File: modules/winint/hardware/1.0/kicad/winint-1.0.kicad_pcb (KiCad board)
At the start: 2 copper layers, 75 x 75 mm, 43 parts, among them J1 NPN SENSOR, J2 Screw_Terminal_01x05, J3 M12-5PIN, J4 RELAYS, K1 SANYOU_SRD_Form_C, K2 SANYOU_SRD_Form_C, Q1 2N2219, Q2 2N2219, SW1 INSTANCE, U1 CNY74-4H, U2 Teensy_3.2, U3 TEC2-2411WI, U4 MCP2551-I-P

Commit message: Refactor again
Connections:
- U2 pad 10: Net-(U1-Pad15) -> Net-(R8-Pad1)
- U2 pad 11: Net-(U1-Pad14) -> Net-(U1-Pad15)
- U2 pad 12: Net-(R8-Pad1) -> Net-(U1-Pad14)
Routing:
- net Net-(R8-Pad1): track 116.8 -> 121.9 mm
- net Net-(U1-Pad15): track 65.1 -> 67.8 mm
- net Net-(U1-Pad14): track 68.5 -> 71.0 mm

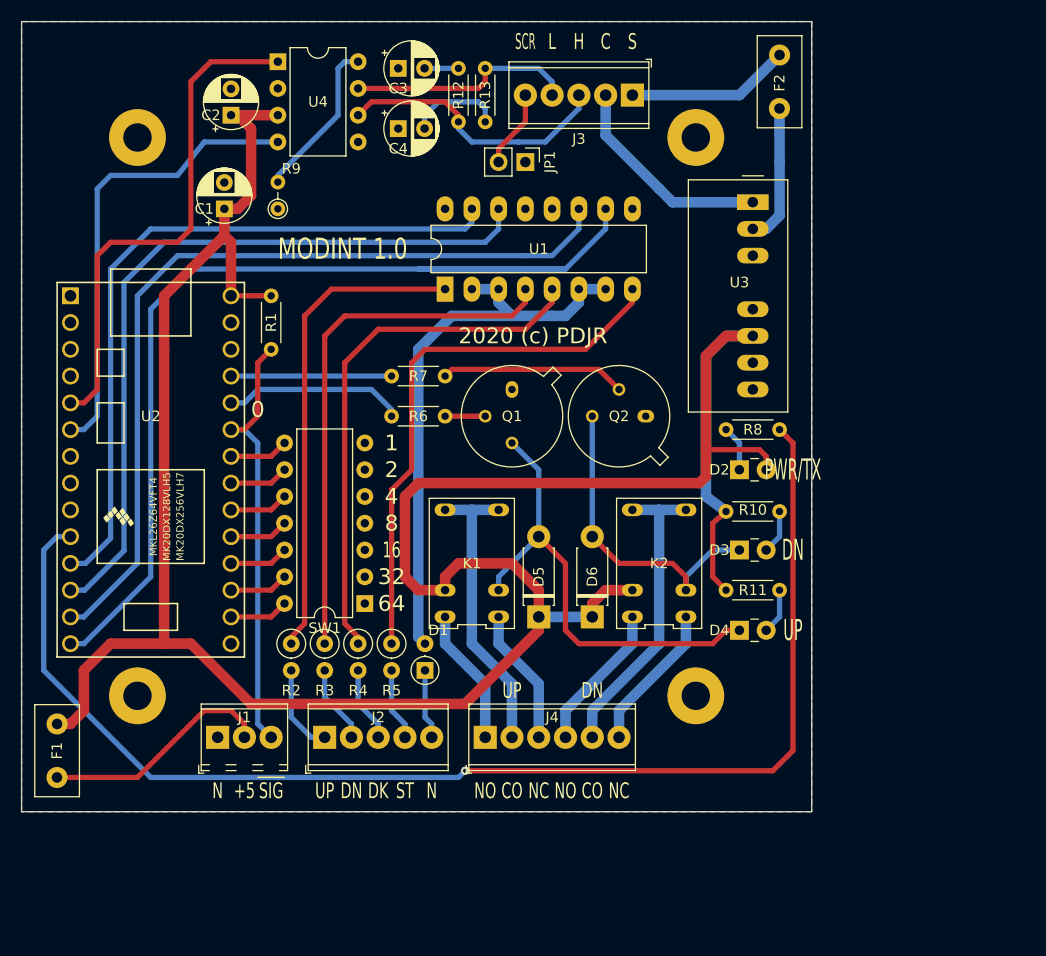
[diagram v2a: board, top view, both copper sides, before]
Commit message: Added 12V fused supply and OPTO isolation to rotation sensor input
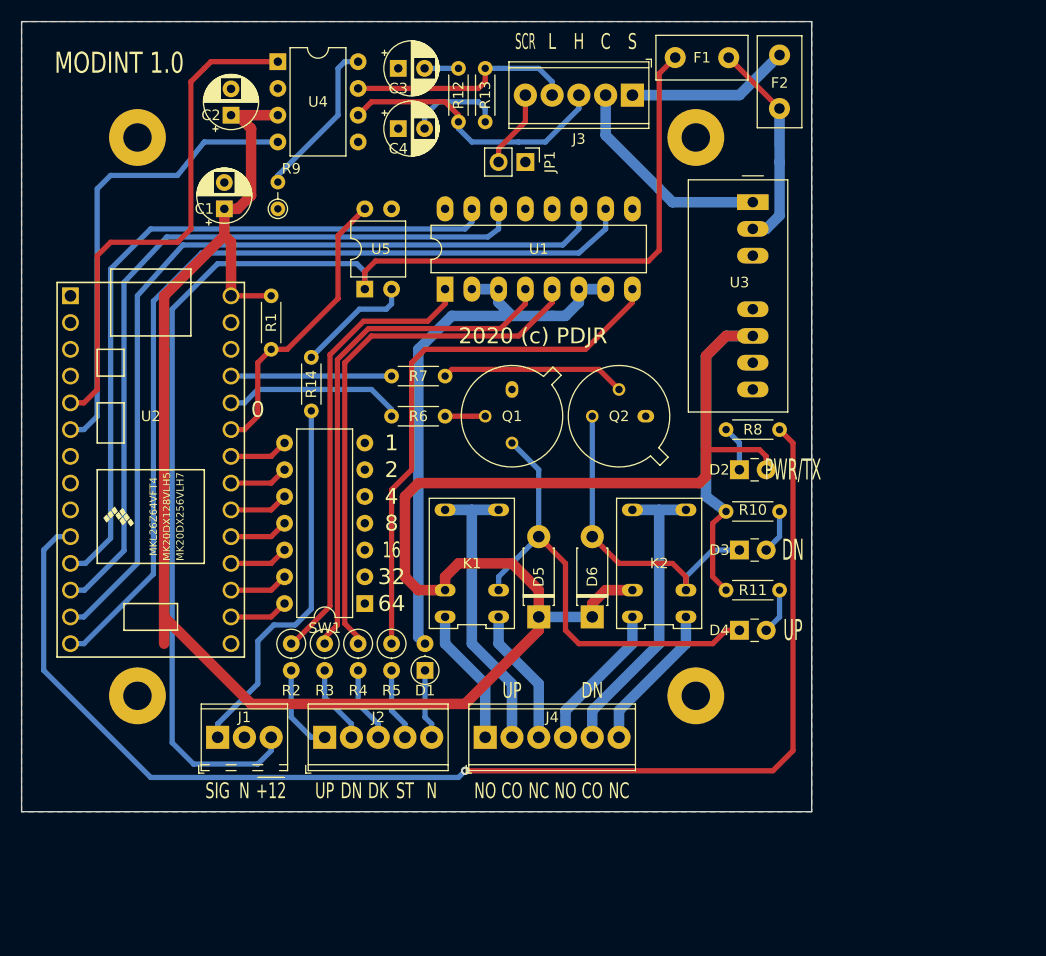
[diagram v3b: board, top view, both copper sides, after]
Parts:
- added R14: 1K, Resistor_THT:R_Axial_DIN0204_L3.6mm_D1.6mm_P5.08mm_Horizontal, F.Cu at (163.5, 124.0)
- added U5: PC817, Package_DIP:DIP-4_W7.62mm, F.Cu at (168.6, 112.4)
- R1: value 4K7 -> 10K
- moved F1 89.8 mm to (203.1, 90.4), turned to 180 degrees
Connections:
- F1 pad 1: Net-(C1-Pad1) -> Net-(F1-Pad1)
- F2 pad 2: Net-(F2-Pad2) -> Net-(F1-Pad1)
- J1 pad 1: GND -> Net-(J1-Pad1)
- J1 pad 2: Net-(F1-Pad2) -> GND
- J1 pad 3: Net-(J1-Pad3) -> Net-(F1-Pad2)
- R1 pad 1: Net-(J1-Pad3) -> Net-(R1-Pad1)
- U2 pad 23: Net-(J1-Pad3) -> Net-(R1-Pad1)
- U3 pad 2: Net-(F2-Pad2) -> Net-(F1-Pad1)
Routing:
- net Net-(F1-Pad2): track 22.2 -> 124.6 mm
- net Net-(J1-Pad3): track 41.5 -> 0.00 mm
- net Net-(J1-Pad1): track 0.00 -> 35.9 mm
- net Net-(R1-Pad1): track 0.00 -> 27.9 mm
- net Net-(F1-Pad1): track 0.00 -> 20.1 mm
- net Net-(C1-Pad1): track 247.1 -> 232.6 mm
- net Net-(U1-Pad10): track 97.2 -> 83.5 mm
- net Net-(F2-Pad2): track 13.2 -> 0.00 mm
- net Net-(R14-Pad2): track 0.00 -> 11.1 mm
- net Net-(R2-Pad1): track 46.0 -> 43.3 mm
- net Net-(R3-Pad1): track 50.8 -> 48.9 mm
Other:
- board text added: "+12"
- board text removed: "+5"

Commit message: Revised for mult-mode inputs
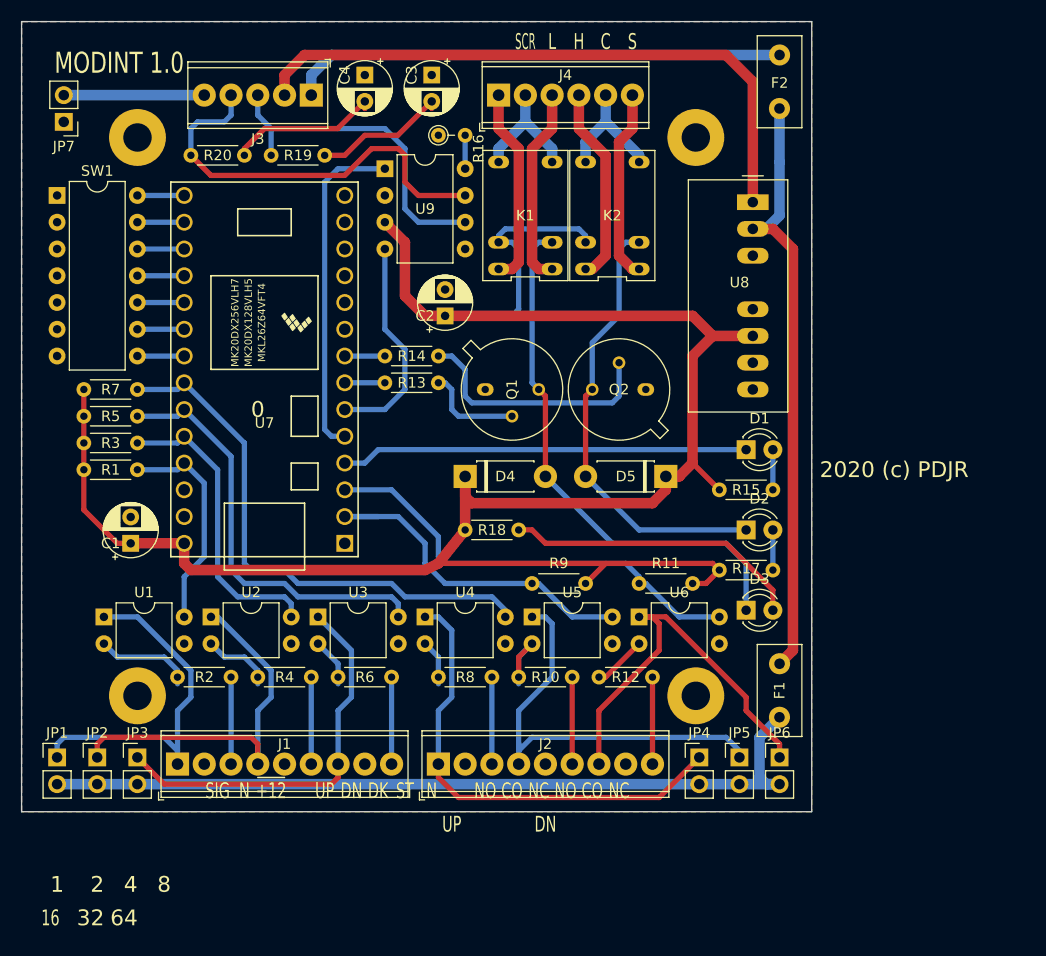
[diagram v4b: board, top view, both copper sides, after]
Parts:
- removed the D1 at (174.3, 148.6)
- removed the R13 at (180.0, 96.5)
- removed the R14 at (163.5, 124.0)
- added JP1: SCR, Connector_PinHeader_2.54mm:PinHeader_1x02_P2.54mm_Vertical, F.Cu at (139.4, 156.8)
- added JP2: SCR, Connector_PinHeader_2.54mm:PinHeader_1x02_P2.54mm_Vertical, F.Cu at (143.2, 156.8)
- added JP3: SCR, Connector_PinHeader_2.54mm:PinHeader_1x02_P2.54mm_Vertical, F.Cu at (147.0, 156.8)
- added JP4: SCR, Connector_PinHeader_2.54mm:PinHeader_1x02_P2.54mm_Vertical, F.Cu at (200.3, 156.8)
- added JP5: SCR, Connector_PinHeader_2.54mm:PinHeader_1x02_P2.54mm_Vertical, F.Cu at (204.1, 156.8)
- added JP6: SCR, Connector_PinHeader_2.54mm:PinHeader_1x02_P2.54mm_Vertical, F.Cu at (207.9, 156.8)
- added R10: 1.4K, Resistor_THT:R_Axial_DIN0204_L3.6mm_D1.6mm_P5.08mm_Horizontal, F.Cu at (183.2, 149.2)
- added R11: 10K, Resistor_THT:R_Axial_DIN0204_L3.6mm_D1.6mm_P5.08mm_Horizontal, F.Cu at (194.6, 140.3)
- added R12: 1.4K, Resistor_THT:R_Axial_DIN0204_L3.6mm_D1.6mm_P5.08mm_Horizontal, F.Cu at (190.8, 149.2)
- added R20: 100R, Resistor_THT:R_Axial_DIN0204_L3.6mm_D1.6mm_P5.08mm_Horizontal, F.Cu at (157.2, 99.7)
- added R6: 1.4K, Resistor_THT:R_Axial_DIN0204_L3.6mm_D1.6mm_P5.08mm_Horizontal, F.Cu at (166.0, 149.2)
- added R7: 10K, Resistor_THT:R_Axial_DIN0204_L3.6mm_D1.6mm_P5.08mm_Horizontal, F.Cu at (147.0, 121.9)
- added R8: 1.4K, Resistor_THT:R_Axial_DIN0204_L3.6mm_D1.6mm_P5.08mm_Horizontal, F.Cu at (175.6, 149.2)
- added R9: 10K, Resistor_THT:R_Axial_DIN0204_L3.6mm_D1.6mm_P5.08mm_Horizontal, F.Cu at (184.5, 140.3)
- added U2: PC817, Package_DIP:DIP-4_W7.62mm, F.Cu at (154.0, 143.5)
- added U3: PC817, Package_DIP:DIP-4_W7.62mm, F.Cu at (164.1, 143.5)
- added U4: PC817, Package_DIP:DIP-4_W7.62mm, F.Cu at (174.3, 143.5)
- added U6: PC817, Package_DIP:DIP-4_W7.62mm, F.Cu at (194.6, 143.5)
- D1: renamed from D2; footprint LED_THT:LED_Rectangular_W3.0mm_H2.0mm -> LED_THT:LED_D3.0mm
- D2: renamed from D3; footprint LED_THT:LED_Rectangular_W3.0mm_H2.0mm -> LED_THT:LED_D3.0mm
- D3: renamed from D4; footprint LED_THT:LED_Rectangular_W3.0mm_H2.0mm -> LED_THT:LED_D3.0mm
- J1: value NPN SENSOR -> Screw_Terminal_01x09; footprint PDJR:TerminalBlock_Phoenix_MPT-0,5-3-2.54_1x03_P2.54mm_Horizontal -> TerminalBlock_Phoenix:TerminalBlock_Phoenix_MPT-0,5-9-2.54_1x09_P2.54mm_Horizontal
- J2: value Screw_Terminal_01x05 -> Screw_Terminal_01x09; footprint TerminalBlock_Phoenix:TerminalBlock_Phoenix_MPT-0,5-5-2.54_1x05_P2.54mm_Horizontal -> TerminalBlock_Phoenix:TerminalBlock_Phoenix_MPT-0,5-9-2.54_1x09_P2.54mm_Horizontal
- R2, R4: value 1K4, 1W -> 1.4K; footprint Resistor_THT:R_Axial_DIN0207_L6.3mm_D2.5mm_P2.54mm_Vertical -> Resistor_THT:R_Axial_DIN0204_L3.6mm_D1.6mm_P5.08mm_Horizontal
- R3, R5: value 1K4, 1W -> 10K; footprint Resistor_THT:R_Axial_DIN0207_L6.3mm_D2.5mm_P2.54mm_Vertical -> Resistor_THT:R_Axial_DIN0204_L3.6mm_D1.6mm_P5.08mm_Horizontal
- U1: value CNY74-4H -> PC817; footprint Package_DIP:DIP-16_W7.62mm_LongPads -> Package_DIP:DIP-4_W7.62mm
- moved J4 61.0 mm to (181.3, 94.0)
- moved F1 57.7 mm to (207.9, 148.0), turned to 270 degrees
- moved SW1 48.5 mm to (139.4, 103.5), turned to 0 degrees
- moved U1 44.9 mm to (143.8, 143.5), turned to 0 degrees
- moved JP7 44.0 mm to (140.0, 96.5), turned to 180 degrees
- moved U5 34.9 mm to (184.5, 143.5), turned to 0 degrees
- moved K1 33.4 mm to (183.8, 105.4)
- moved K2 33.3 mm to (192.1, 105.4)
- moved C1 33.0 mm to (146.4, 136.5)
- moved R5 32.4 mm to (147.0, 124.5), turned to 180 degrees
- moved J3 30.5 mm to (163.5, 94.0)
- moved C2 27.9 mm to (176.2, 114.9)
- moved R3 26.1 mm to (147.0, 127.0), turned to 180 degrees
- moved R18 25.4 mm to (183.2, 135.3)
- moved R19 18.1 mm to (159.7, 99.7), turned to 0 degrees
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- renumbered D5 to D4, D6 to D5, JP1 to JP7, R6 to R13, R7 to R14, R8 to R15, R9 to R16, R10 to R17, R11 to R18, R12 to R19, U2 to U7, U3 to U8, U4 to U9
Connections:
- D1 pad 1: Net-(D2-Pad1) (its old number) -> Net-(D1-Pad1)
- D1 pad 2: Net-(C1-Pad1) -> Net-(D1-Pad2)
- J1 pad 3: Net-(F1-Pad2) -> Net-(J1-Pad3)
- J2 pad 2: Net-(J2-Pad2) -> GND
- J2 pad 5: Net-(D1-Pad1) -> GND
- R13 pad 2: Net-(R6-Pad2) -> Net-(R13-Pad2)
- R14 pad 2: Net-(R7-Pad2) -> Net-(R14-Pad2)
- R15 pad 1: Net-(R8-Pad1) -> Net-(D1-Pad2)
- R15 pad 2: Net-(D2-Pad1) (its old number) -> Net-(C1-Pad1)
- R2 pad 2: Net-(J2-Pad1) -> Net-(J1-Pad3)
- R3 pad 2: Net-(J2-Pad2) -> Net-(C1-Pad1)
- R4 pad 2: Net-(J2-Pad3) -> Net-(J1-Pad6)
- R5 pad 2: Net-(J2-Pad4) -> Net-(C1-Pad1)
- U1 pad 1: Net-(R2-Pad1) -> Net-(J1-Pad1)
- U1 pad 2: Net-(D1-Pad2) -> Net-(R2-Pad1)
- U1 pad 3: Net-(D1-Pad2) -> GND
- U1 pad 4: Net-(R3-Pad1) -> Net-(R1-Pad1)
- U5 pad 1: Net-(F1-Pad2) -> Net-(J2-Pad4)
- U5 pad 4: Net-(R1-Pad1) -> Net-(R9-Pad1)
- U7 pad 10: Net-(R8-Pad1) -> (no net)
- U7 pad 11: Net-(U1-Pad15) -> (no net)
- U7 pad 12: Net-(U1-Pad14) -> (no net)
- U7 pad 13: Net-(U1-Pad11) -> (no net)
- U7 pad 14: Net-(U1-Pad10) -> (no net)
- U7 pad 15: (no net) -> Net-(SW1-Pad14)
- U7 pad 16: Net-(SW1-Pad14) -> Net-(SW1-Pad13)
- U7 pad 17: Net-(SW1-Pad13) -> Net-(SW1-Pad12)
- U7 pad 18: Net-(SW1-Pad12) -> Net-(SW1-Pad11)
- U7 pad 19: Net-(SW1-Pad11) -> Net-(SW1-Pad10)
- U7 pad 2: (no net) -> Net-(R9-Pad1)
- U7 pad 20: Net-(SW1-Pad10) -> Net-(SW1-Pad9)
- U7 pad 21: Net-(SW1-Pad9) -> Net-(SW1-Pad8)
- U7 pad 22: Net-(SW1-Pad8) -> Net-(R7-Pad1)
- U7 pad 23: Net-(R1-Pad1) -> Net-(R5-Pad1)
- U7 pad 24: Net-(R6-Pad2) -> Net-(R3-Pad1)
- U7 pad 25: Net-(R7-Pad2) -> Net-(R1-Pad1)
- U7 pad 3: (no net) -> Net-(R11-Pad1)
- U7 pad 4: (no net) -> Net-(D1-Pad1)
- U7 pad 7: (no net) -> Net-(R13-Pad2)
- U7 pad 8: (no net) -> Net-(R14-Pad2)
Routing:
- net Net-(R8-Pad1): track 121.9 -> 4.34 mm, vias 1 -> 0
- net Net-(U1-Pad10): track 83.5 -> 0.00 mm
- net Net-(U1-Pad11): track 80.5 -> 0.00 mm
- net Net-(U1-Pad14): track 71.0 -> 0.00 mm
- net Net-(U1-Pad15): track 67.8 -> 0.00 mm
- net Net-(R7-Pad1): track 0.00 -> 51.5 mm
- net Net-(D1-Pad2): track 54.7 -> 3.81 mm
- net Net-(F1-Pad2): track 124.6 -> 77.3 mm
- net Net-(R4-Pad1): track 50.5 -> 6.77 mm
- net Net-(R11-Pad1): track 0.00 -> 42.0 mm
- net Net-(J3-Pad2): track 20.4 -> 59.6 mm
- net Net-(J2-Pad7): track 0.00 -> 38.2 mm
- net Net-(F1-Pad1): track 20.1 -> 57.7 mm
- net Net-(J1-Pad7): track 0.00 -> 36.8 mm
- net Net-(J1-Pad4): track 0.00 -> 36.3 mm
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
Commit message: Revised PCB layout
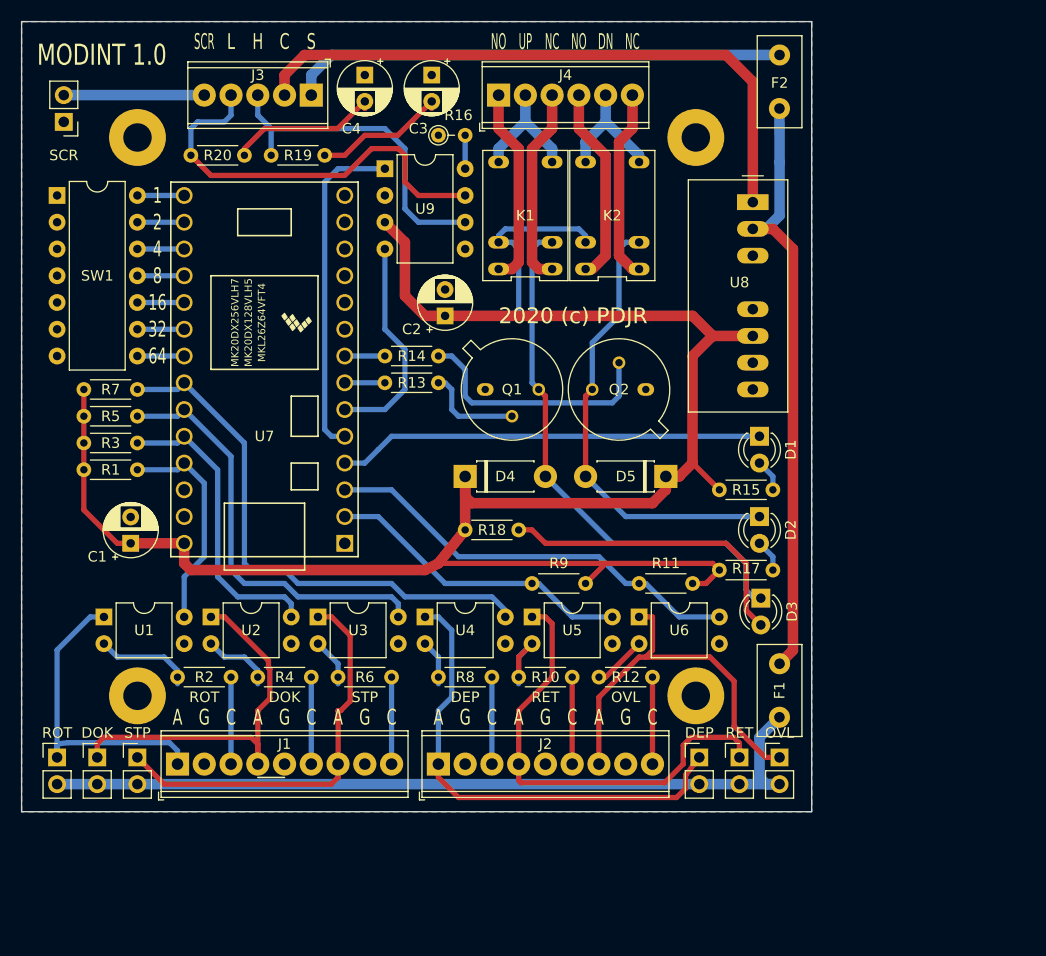
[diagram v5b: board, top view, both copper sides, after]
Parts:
- U1: value PC817 -> ROT
- U2: value PC817 -> DOK
- U3: value PC817 -> STP
- U4: value PC817 -> DEP
- U5: value PC817 -> RET
- U6: value PC817 -> OVL
- moved D3 1.81 mm to (206.2, 141.7), turned to 270 degrees
- moved D1 1.80 mm to (206.0, 126.4), turned to 270 degrees
- moved D2 1.80 mm to (206.0, 134.0), turned to 270 degrees
- renumbered JP4 to DEP, JP2 to DOK, JP6 to OVL, JP5 to RET, JP1 to ROT, JP7 to SCR, JP3 to STP
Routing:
- net Net-(R9-Pad1): track 33.6 -> 29.3 mm
- net Net-(J2-Pad4): track 40.1 -> 43.8 mm
- net Net-(J1-Pad1): track 33.3 -> 30.2 mm
- net Net-(D1-Pad1): track 38.6 -> 40.4 mm
- net Net-(R11-Pad1): track 42.0 -> 40.6 mm
- net Net-(J1-Pad7): track 36.8 -> 38.3 mm
- net Net-(J2-Pad7): track 38.2 -> 36.9 mm
- net Net-(D3-Pad2): track 28.4 -> 29.3 mm
- net Net-(J2-Pad1): track 44.1 -> 44.9 mm
- net Net-(D3-Pad1): track 51.8 -> 51.0 mm
- net Net-(D2-Pad2): track 3.81 -> 3.07 mm
- net Net-(D2-Pad1): track 42.4 -> 43.2 mm
- net Net-(D1-Pad2): track 3.81 -> 3.07 mm
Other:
- board text added: "A"
- board text added: "G"
- board text removed: "+12"
- board text removed: "0"
- board text removed: "CO"
- board text removed: "DK"
- board text removed: "N"
- board text removed: "SIG"
- board text removed: "ST"

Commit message: Tidy up
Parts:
- R15: value 200R, 125mW -> 200R
- renumbered ROT to JP1, DOK to JP2, STP to JP3, DEP to JP4, RET to JP5, OVL to JP6, SCR to JP7
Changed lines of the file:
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@@
-(kicad_pcb (version 20171130) (host pcbnew 5.1.5-52549c5~84~ubuntu18.04.1)
+(kicad_pcb (version 20171130) (host pcbnew 5.1.5-1.fc31)
   (general
     (thickness 1.6)
@@
   )
   (layers
-    (0 F.Cu signal hide)
-    (31 B.Cu signal hide)
+    (0 F.Cu signal)
+    (31 B.Cu signal)
     (33 F.Adhes user)
     (35 F.Paste user hide)
@@
   )
   (setup
-    (last_trace_width 0.5)
+    (last_trace_width 0.25)
     (user_trace_width 0.5)
     (user_trace_width 1)
@@
     (descr "Through hole straight pin header, 1x02, 2.54mm pitch, single row")
     (tags "Through hole pin header THT 1x02 2.54mm single row")
-    (fp_text reference OVL (at 0 -2.33) (layer F.SilkS)
+    (fp_text reference JP6 (at 0 -2.33) (layer F.SilkS)
       (effects (font (size 1 1) (thickness 0.15)))
     )
@@
     (descr "Through hole straight pin header, 1x02, 2.54mm pitch, single row")
     (tags "Through hole pin header THT 1x02 2.54mm single row")
-    (fp_text reference RET (at 0 -2.33) (layer F.SilkS)
+    (fp_text reference JP5 (at 0 -2.33) (layer F.SilkS)
       (effects (font (size 1 1) (thickness 0.15)))
     )
@@
     (descr "Through hole straight pin header, 1x02, 2.54mm pitch, single row")
     (tags "Through hole pin header THT 1x02 2.54mm single row")
-    (fp_text reference DEP (at 0 -2.33) (layer F.SilkS)
+    (fp_text reference JP4 (at 0 -2.33) (layer F.SilkS)
       (effects (font (size 1 1) (thickness 0.15)))
     )
@@
     (descr "Through hole straight pin header, 1x02, 2.54mm pitch, single row")
     (tags "Through hole pin header THT 1x02 2.54mm single row")
-    (fp_text reference STP (at 0 -2.33) (layer F.SilkS)
+    (fp_text reference JP3 (at 0 -2.33) (layer F.SilkS)
       (effects (font (size 1 1) (thickness 0.15)))
     )
@@
     (descr "Through hole straight pin header, 1x02, 2.54mm pitch, single row")
     (tags "Through hole pin header THT 1x02 2.54mm single row")
-    (fp_text reference DOK (at 0 -2.33) (layer F.SilkS)
+    (fp_text reference JP2 (at 0 -2.33) (layer F.SilkS)
       (effects (font (size 1 1) (thickness 0.15)))
     )
@@
     (descr "Through hole straight pin header, 1x02, 2.54mm pitch, single row")
     (tags "Through hole pin header THT 1x02 2.54mm single row")
-    (fp_text reference ROT (at 0 -2.33) (layer F.SilkS)
+    (fp_text reference JP1 (at 0 -2.33) (layer F.SilkS)
       (effects (font (size 1 1) (thickness 0.15)))
     )
@@
     (descr "Through hole straight pin header, 1x02, 2.54mm pitch, single row")
     (tags "Through hole pin header THT 1x02 2.54mm single row")
-    (fp_text reference SCR (at 0 -3.175) (layer F.SilkS)
+    (fp_text reference JP7 (at 0 -3.175) (layer F.SilkS)
       (effects (font (size 1 1) (thickness 0.15)))
     )
@@
       (effects (font (size 1 1) (thickness 0.15)))
     )
-    (fp_text value "200R, 125mW" (at 2.54 1.92) (layer F.Fab) hide
-      (effects (font (size 1 1) (thickness 0.15)))
-    )
+    (fp_text value 200R (at 2.54 1.92) (layer F.Fab) hide
+      (effects (font (size 1 1) (thickness 0.15)))
+    )
